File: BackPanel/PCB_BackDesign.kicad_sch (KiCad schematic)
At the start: 25 parts, among them J1 Molex Picoblade 0530470810, J2 Molex Picoblade 0530470910, J3 B2B-PH-K-S, J4 B2B-PH-K-S, SW1 KS11R23CQD (red), SW2 KS11R22CQD (black), SW3 KS11R27CQD (blue)

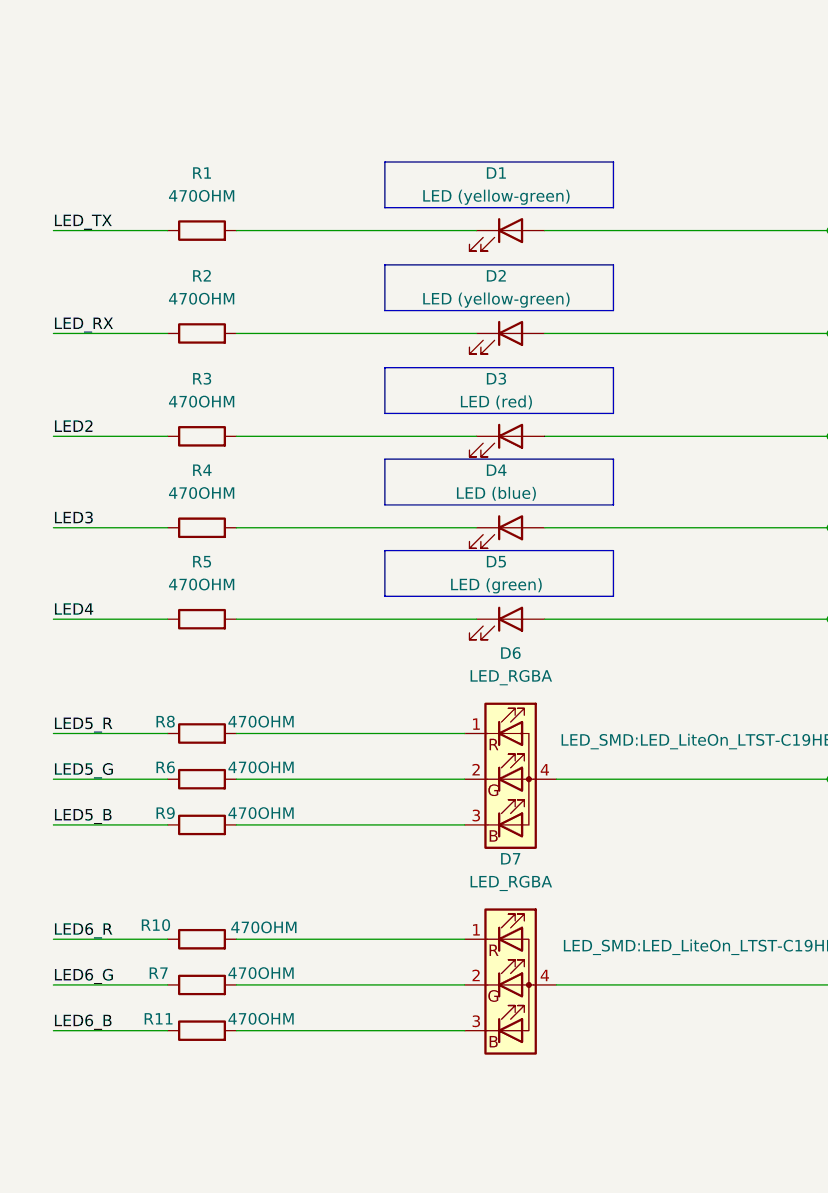
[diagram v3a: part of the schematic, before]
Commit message: Added a readme file; added part numbers to the schematic.
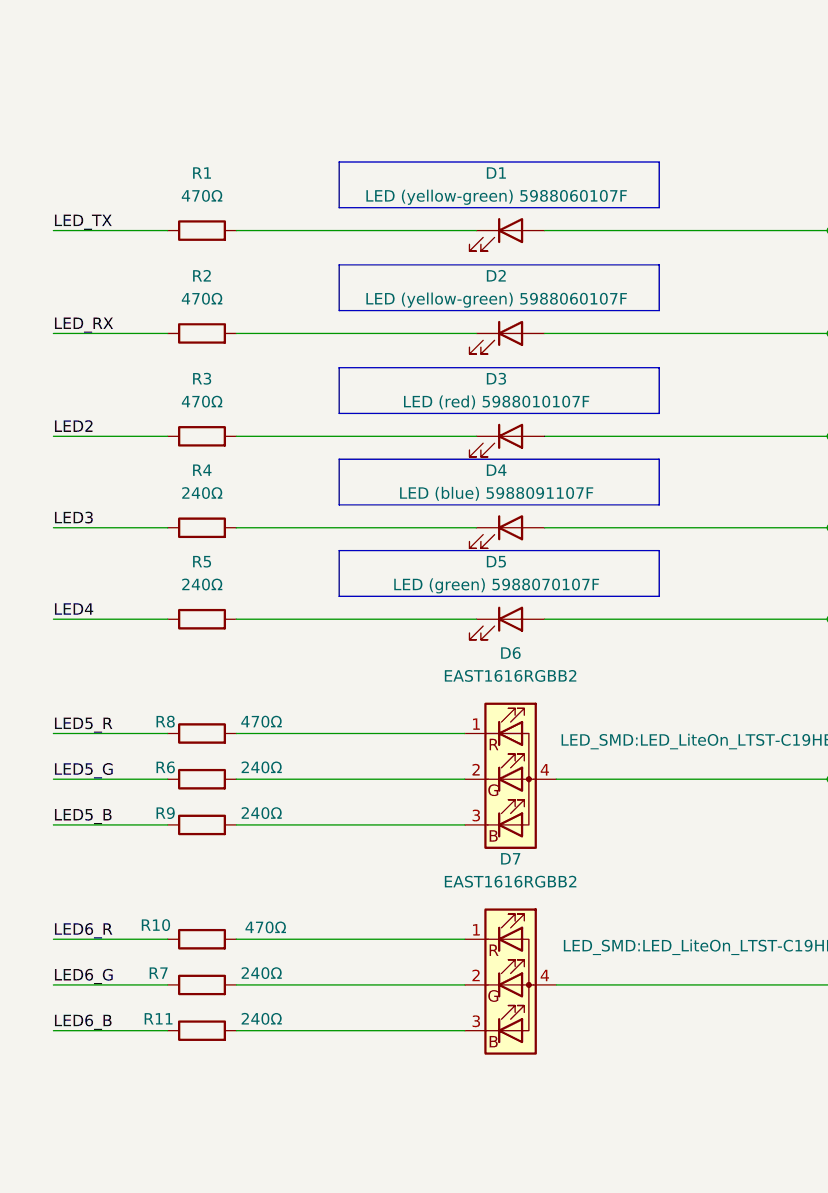
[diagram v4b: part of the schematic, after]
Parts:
- D1, D2: value LED (yellow-green) -> LED (yellow-green) 5988060107F
- D3: value LED (red) -> LED (red) 5988010107F
- D4: value LED (blue) -> LED (blue) 5988091107F
- D5: value LED (green) -> LED (green) 5988070107F
- D6, D7: value LED_RGBA -> EAST1616RGBB2
- R1, R10, R2, R3, R8: value 470OHM -> 470Ω
- R11, R4, R5, R6, R7, R9: value 470OHM -> 240Ω
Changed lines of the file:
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@@
 	)
 	(rectangle
-		(start 204.47 63.5)
-		(end 229.87 68.58)
+		(start 199.39 63.5)
+		(end 234.95 68.58)
 		(stroke
 			(width 0)
@@
 	)
 	(rectangle
-		(start 204.47 74.93)
-		(end 229.87 80.01)
+		(start 199.39 74.93)
+		(end 234.95 80.01)
 		(stroke
 			(width 0)
@@
 	)
 	(rectangle
-		(start 204.47 85.09)
-		(end 229.87 90.17)
+		(start 199.39 85.09)
+		(end 234.95 90.17)
 		(stroke
 			(width 0)
@@
 	)
 	(rectangle
-		(start 204.47 95.25)
-		(end 229.87 100.33)
+		(start 199.39 95.25)
+		(end 234.95 100.33)
 		(stroke
 			(width 0)
@@
 	)
 	(rectangle
-		(start 204.47 52.07)
-		(end 229.87 57.15)
+		(start 199.39 52.07)
+		(end 234.95 57.15)
 		(stroke
 			(width 0)
@@
 			)
 		)
-		(property "Value" "LED (green)"
+		(property "Value" "LED (green) 5988070107F"
 			(at 216.8525 99.06 0)
 			(effects
@@
 			)
 		)
-		(property "Datasheet" "~"
+		(property "Datasheet" "https://s3-us-west-2.amazonaws.com/catsy.557/Dialight_CBI_data_598-0603_Apr2018.pdf"
 			(at 218.44 102.87 0)
 			(effects
@@
 			)
 		)
-		(property "Value" "470OHM"
-			(at 194.818 137.16 90)
+		(property "Value" "470Ω"
+			(at 193.548 137.16 90)
 			(effects
 				(font
@@
 			)
 		)
-		(property "Value" "470OHM"
+		(property "Value" "470Ω"
 			(at 184.15 67.31 90)
 			(effects
@@
 			)
 		)
-		(property "Value" "LED (yellow-green)"
+		(property "Value" "LED (yellow-green) 5988060107F"
 			(at 216.8525 55.88 0)
 			(effects
@@
 			)
 		)
-		(property "Datasheet" "~"
+		(property "Datasheet" "https://s3-us-west-2.amazonaws.com/catsy.557/Dialight_CBI_data_598-0603_Apr2018.pdf"
 			(at 218.44 59.69 0)
 			(effects
@@
 			)
 		)
-		(property "Value" "LED (yellow-green)"
+		(property "Value" "LED (yellow-green) 5988060107F"
 			(at 216.8525 67.31 0)
 			(effects
@@
 			)
 		)
-		(property "Datasheet" "~"
+		(property "Datasheet" "https://s3-us-west-2.amazonaws.com/catsy.557/Dialight_CBI_data_598-0603_Apr2018.pdf"
 			(at 218.44 71.12 0)
 			(effects
@@
 			)
 		)
-		(property "Value" "LED (red)"
+		(property "Value" "LED (red) 5988010107F"
 			(at 216.8525 78.74 0)
 			(effects
@@
 			)
 		)
-		(property "Datasheet" "~"
+		(property "Datasheet" "https://s3-us-west-2.amazonaws.com/catsy.557/Dialight_CBI_data_598-0603_Apr2018.pdf"
 			(at 218.44 82.55 0)
 			(effects
@@
 			)
 		)
-		(property "Value" "470OHM"
+		(property "Value" "240Ω"
 			(at 190.754 124.46 90)
 			(effects
@@
 			)
 		)
-		(property "Value" "LED (blue)"
+		(property "Value" "LED (blue) 5988091107F"
 			(at 216.8525 88.9 0)
 			(effects
@@
 			)
 		)
-		(property "Datasheet" "~"
+		(property "Datasheet" "https://s3-us-west-2.amazonaws.com/catsy.557/Dialight_CBI_data_598-0603_Apr2018.pdf"
 			(at 218.44 92.71 0)
 			(effects
@@
 			)
 		)
-		(property "Value" "470OHM"
+		(property "Value" "240Ω"
 			(at 190.754 147.32 90)
 			(effects
@@
 			)
 		)
-		(property "Value" "470OHM"
+		(property "Value" "470Ω"
 			(at 184.15 78.74 90)
 			(effects
@@
 			)
 		)
-		(property "Value" "LED_RGBA"
+		(property "Value" "EAST1616RGBB2"
 			(at 218.44 132.08 0)
 			(effects
@@
 			)
 		)
-		(property "Value" "470OHM"
+		(property "Value" "240Ω"
 			(at 190.754 142.24 90)
 			(effects
@@
 			)
 		)
-		(property "Value" "470OHM"
+		(property "Value" "240Ω"
 			(at 190.754 119.38 90)
 			(effects
@@
 			)
 		)
-		(property "Value" "470OHM"
+		(property "Value" "240Ω"
 			(at 184.15 99.06 90)
 			(effects
@@
 			)
 		)
-		(property "Value" "470OHM"
+		(property "Value" "240Ω"
 			(at 184.15 88.9 90)
 			(effects
@@
 			)
 		)
-		(property "Value" "LED_RGBA"
+		(property "Value" "EAST1616RGBB2"
 			(at 218.44 109.22 0)
 			(effects
@@
 			)
 		)
-		(property "Value" "470OHM"
+		(property "Value" "470Ω"
 			(at 190.754 114.3 90)
 			(effects
@@
 			)
 		)
-		(property "Value" "470OHM"
+		(property "Value" "470Ω"
 			(at 184.15 55.88 90)
 			(effects

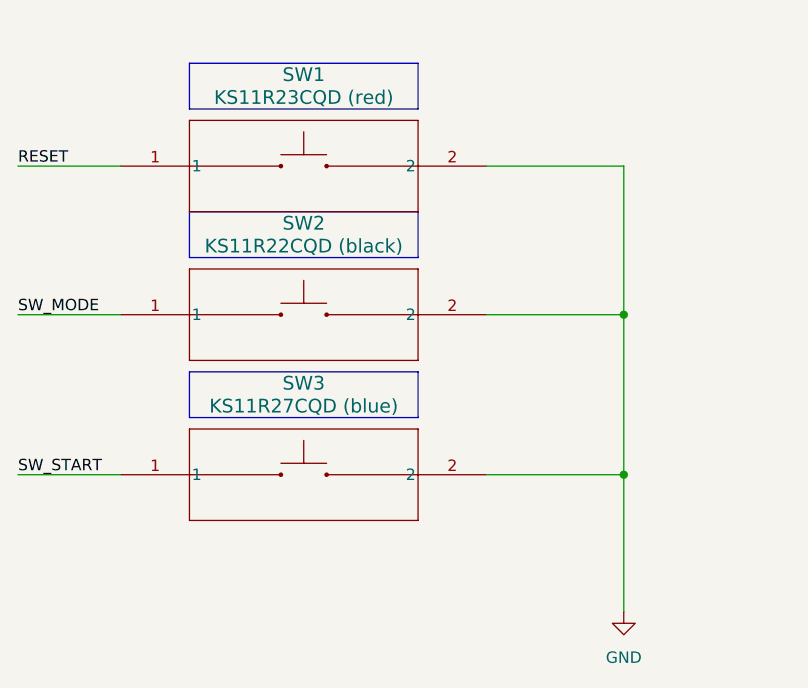
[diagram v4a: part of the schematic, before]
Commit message: Added three debouncing capacitors.
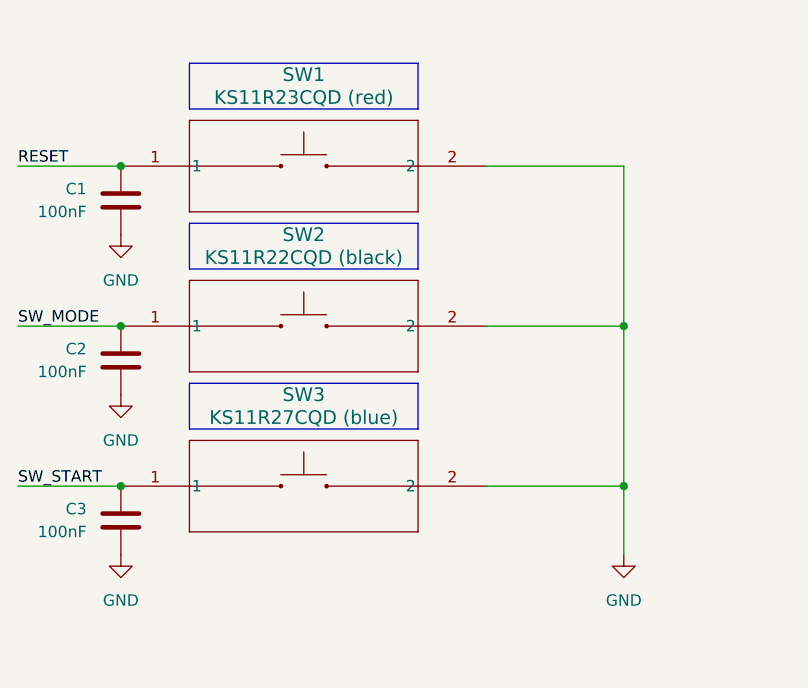
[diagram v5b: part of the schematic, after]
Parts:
- added C1, C2, C3: 100nF, Capacitor_SMD:C_0603_1608Metric, symbol Device:C
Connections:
- net GND: now also C1.2, C2.2, C3.2
- net RESET: now also C1.1
- net SW_MODE: now also C2.1
- net SW_START: now also C3.1
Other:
- moved on the sheet: SW2, SW3
